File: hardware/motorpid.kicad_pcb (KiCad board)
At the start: 2 copper layers, 170 x 120 mm, 110 parts, among them J1 BNC, J2 BNC, J3 BNC, J4 MOTOR + - shield, J5 POT 1 (+) 2 (wiper) 3 (-), J6 +15 / GND / -15, Q1 MJB44H11, Q2 MJB45H11, SW1 TARGET SOURCE, SW2 LOOP, SW3 D IN / OFF, SW4 I IN / OFF, SW5 D CAPACITOR, U1 LM321, U2 LM321, U3 LM321, U4 LM321, U5 LM321, U6 LM321, U7 LM321

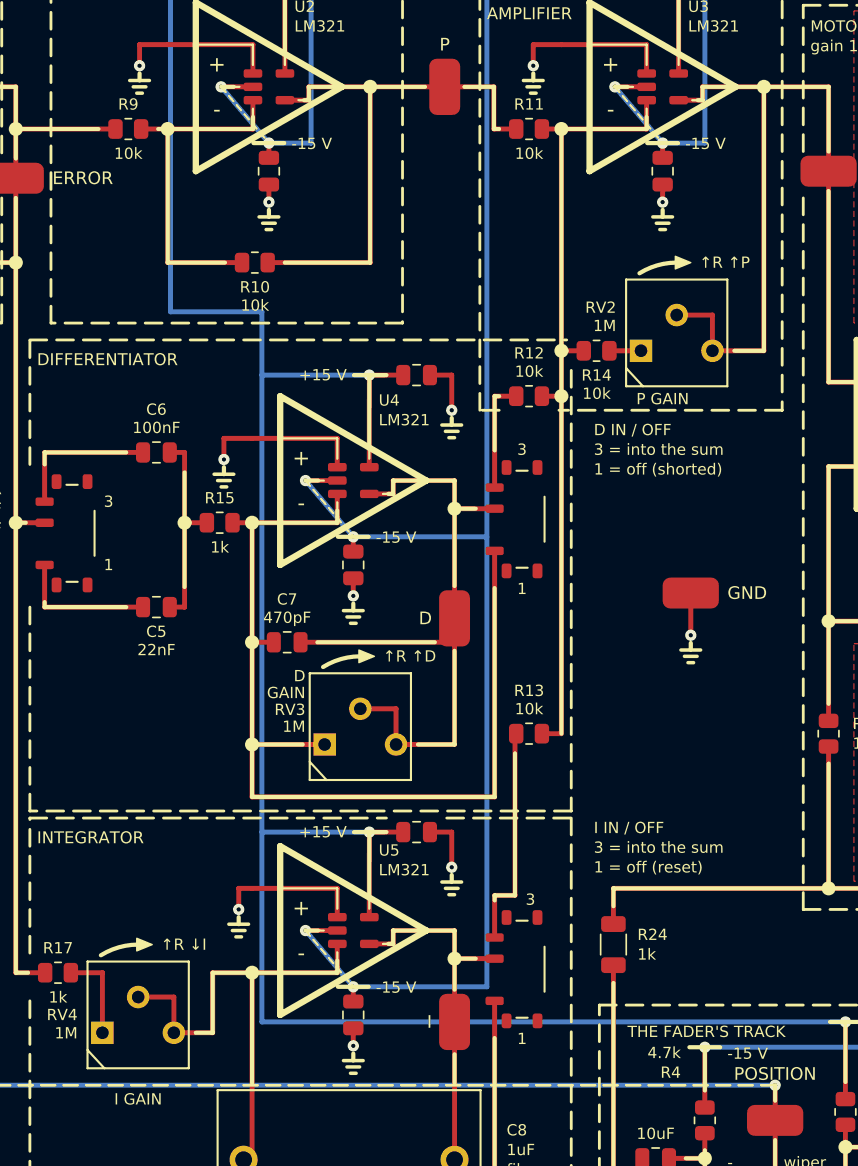
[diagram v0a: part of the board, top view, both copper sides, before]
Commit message: JLCPCB's preview read back: the 3362P's body 1.30 mm toward pins 1 and 3 (BOCHEN's drawing; outline, courtyard, model; RV2 with R14 up 1.1 mm, RV4 up 0.5), the MSK12C02 placed by its body (datum 0.55 mm; the knob sideways, in the courtyard and the model); check_rotations.py lays JLCPCB's 3D bodies on our courtyards; chat log Response 15
Co-Authored-By: Claude Opus 5.5 <noreply@anthropic.com>
Claude-Session: https://claude.ai/code/session_017Q2PYKR2UewvTfQgKmRJsG
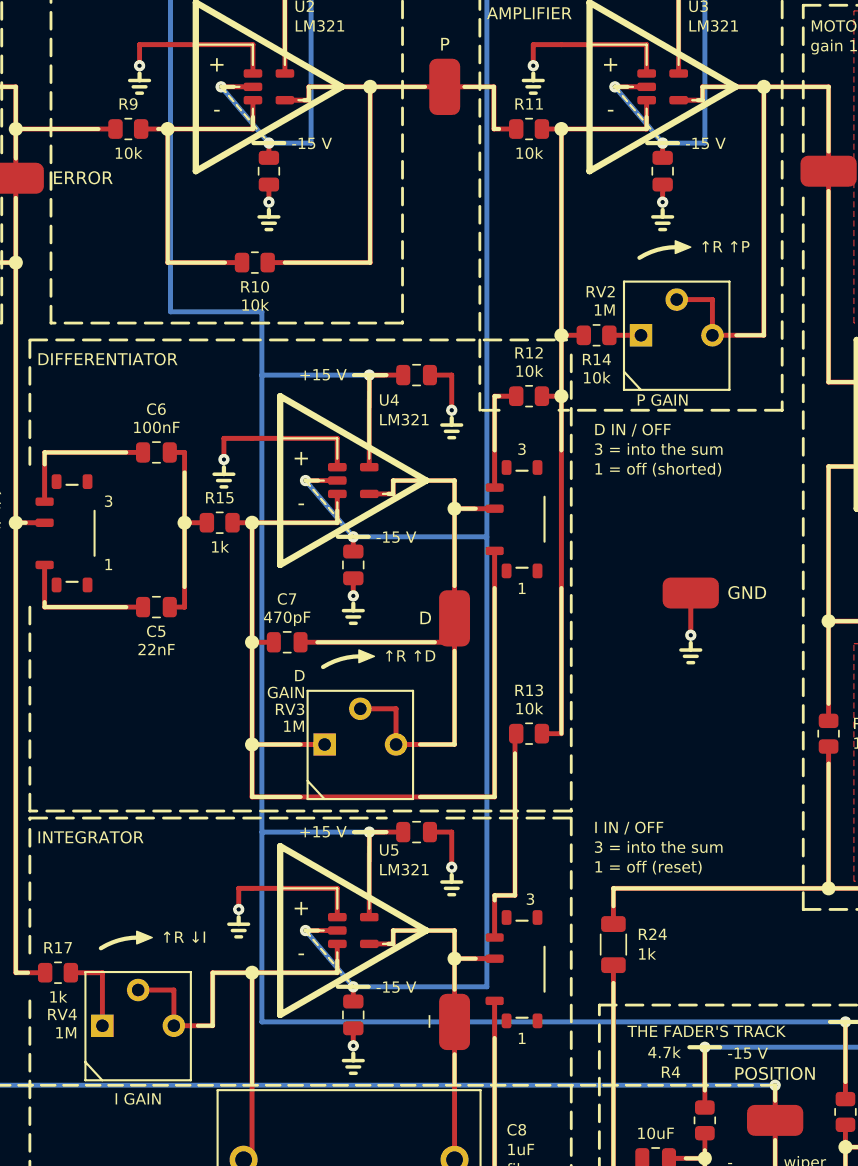
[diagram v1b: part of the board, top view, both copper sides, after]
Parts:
- moved RV2 1.10 mm to (117.0, 50.4)
- moved R14 1.10 mm to (111.3, 51.7)
- moved RV4 0.50 mm to (78.7, 99.5)
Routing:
- net /SUM: track 68.2 -> 67.1 mm
- net Net-(SW4-A): track 78.1 -> 77.6 mm
- net Net-(R17-Pad2): track 6.52 -> 6.02 mm
